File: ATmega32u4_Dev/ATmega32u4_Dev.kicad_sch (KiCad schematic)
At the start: 32 parts, among them J1 USB4105-GF-A, J2 ICSP HEader 2x3, J3 Conn_01x14_Pin, J4 Conn_01x14_Pin, SW1 1825910-6, U1 ATmega32U4-A, Y1 ABM8-16.000MHZ-10-1-U-T

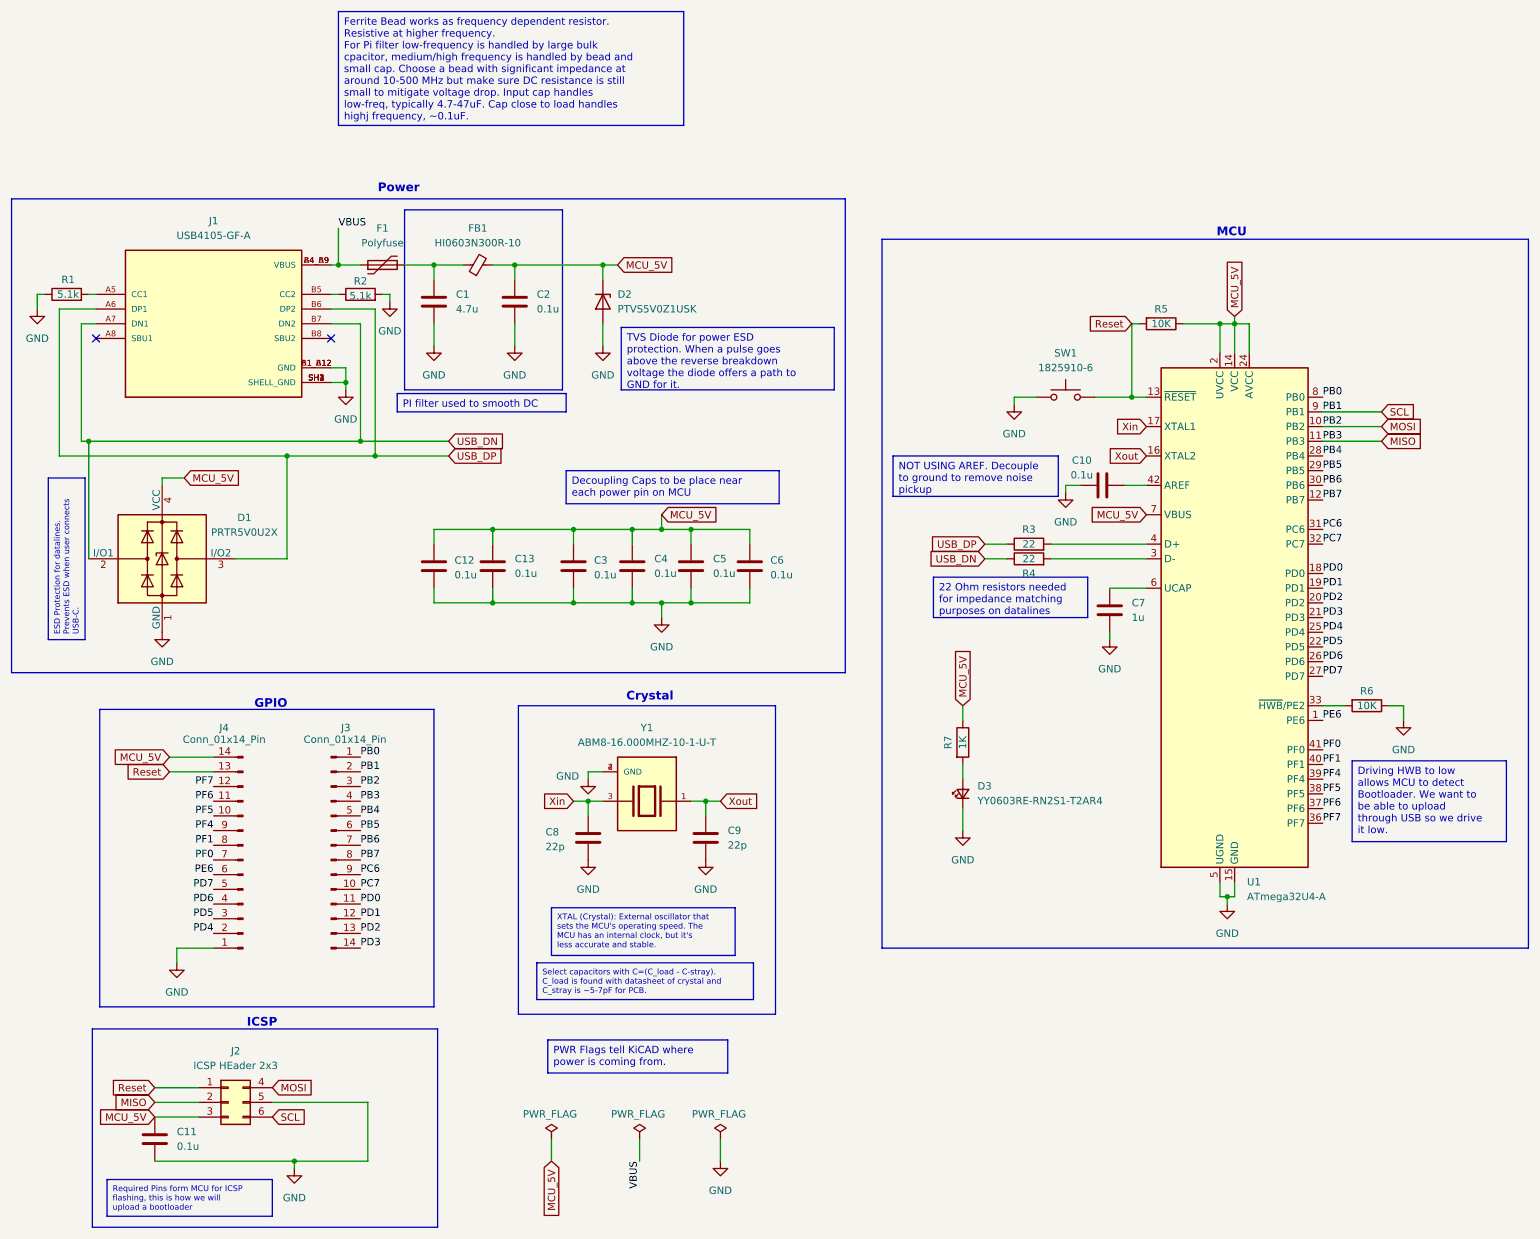
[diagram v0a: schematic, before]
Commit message: changed GPIO
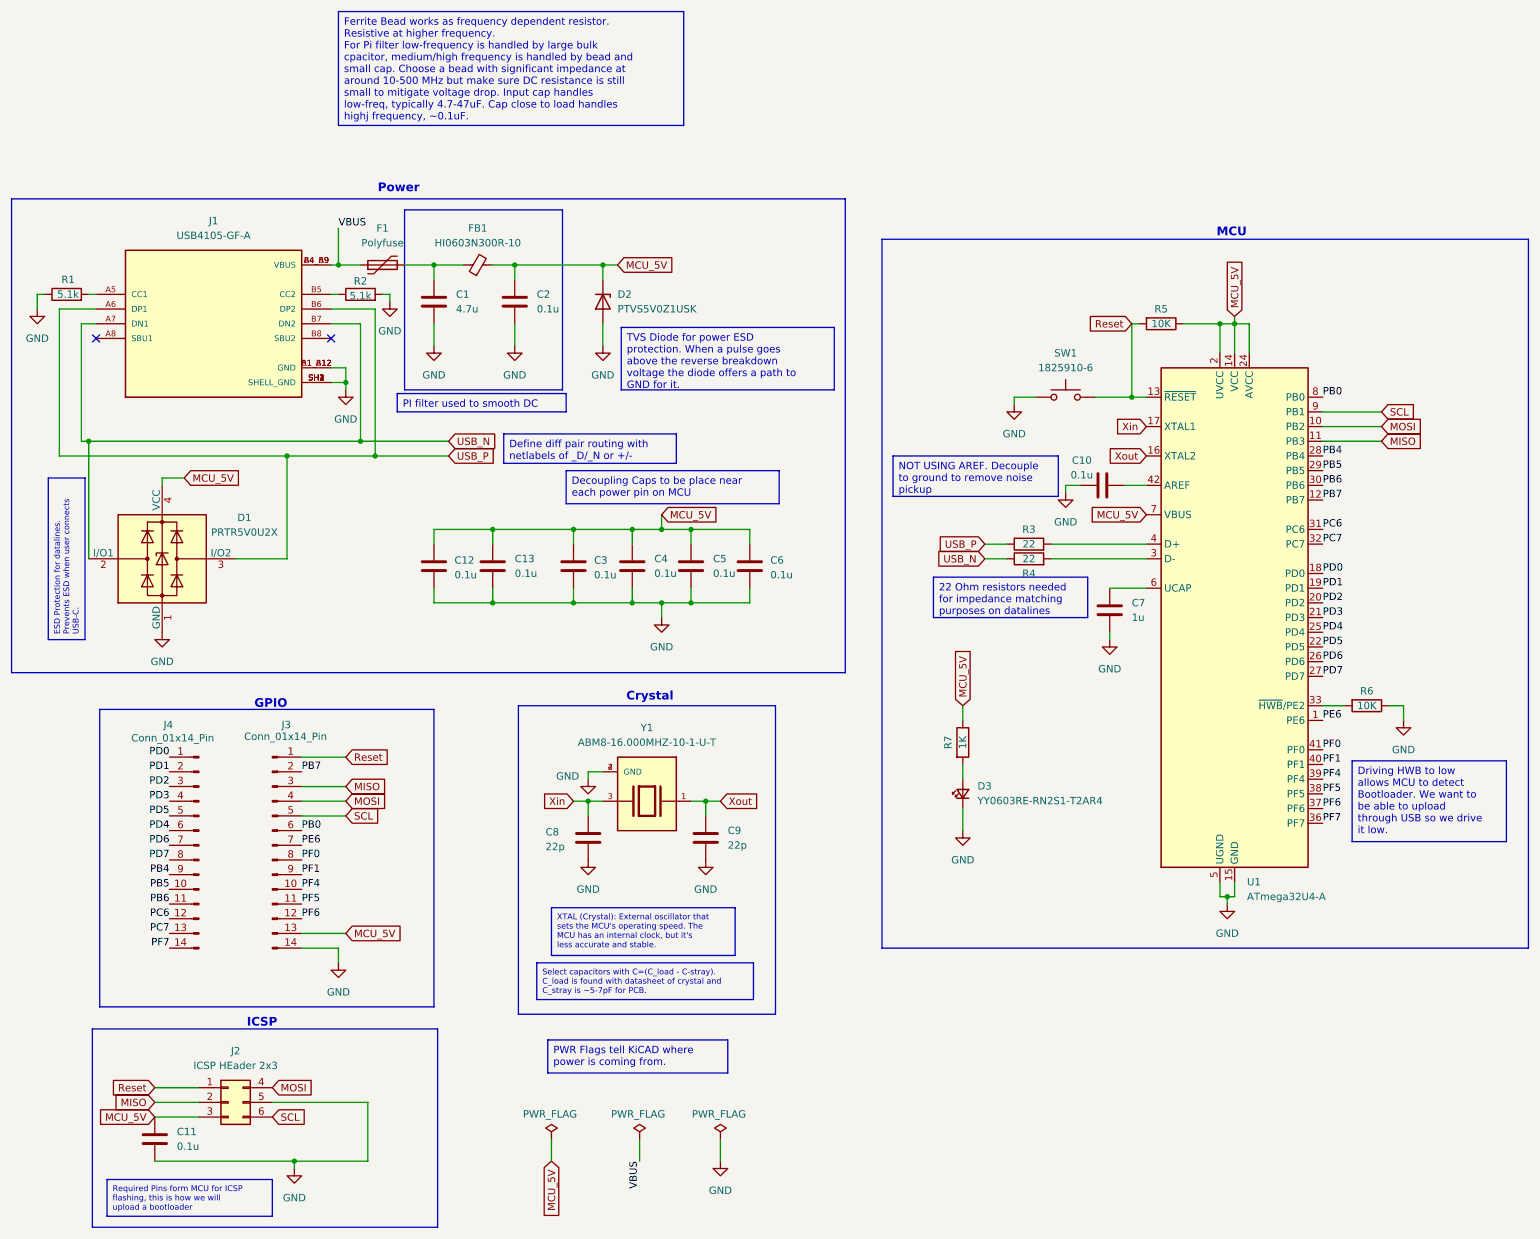
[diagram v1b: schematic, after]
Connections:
- net GND: now also J3.14 (Pin_14); no longer J4.1 (Pin_1)
- net MCU_5V: now also J3.13 (Pin_13); no longer J4.14 (Pin_14)
- net MISO: now also J3.3 (Pin_3); no longer J3.4 (Pin_4)
- net MOSI: now also J3.4 (Pin_4); no longer J3.3 (Pin_3)
- net PB0: now also J3.6 (Pin_6); no longer J3.1 (Pin_1)
- net PB4: now also J4.9 (Pin_9); no longer J3.5 (Pin_5)
- net PB5: now also J4.10 (Pin_10); no longer J3.6 (Pin_6)
- net PB6: now also J4.11 (Pin_11); no longer J3.7 (Pin_7)
- net PB7: now also J3.2 (Pin_2); no longer J3.8 (Pin_8)
- net PC6: now also J4.12 (Pin_12); no longer J3.9 (Pin_9)
- net PC7: now also J4.13 (Pin_13); no longer J3.10 (Pin_10)
- net PD0: now also J4.1 (Pin_1); no longer J3.11 (Pin_11)
- net PD1: now also J4.2 (Pin_2); no longer J3.12 (Pin_12)
- net PD2: now also J4.3 (Pin_3); no longer J3.13 (Pin_13)
- net PD3: now also J4.4 (Pin_4); no longer J3.14 (Pin_14)
- net PD4: now also J4.6 (Pin_6); no longer J4.2 (Pin_2)
- net PD5: now also J4.5 (Pin_5); no longer J4.3 (Pin_3)
- net PD6: now also J4.7 (Pin_7); no longer J4.4 (Pin_4)
- net PD7: now also J4.8 (Pin_8); no longer J4.5 (Pin_5)
- net PE6: now also J3.7 (Pin_7); no longer J4.6 (Pin_6)
- net PF0: now also J3.8 (Pin_8); no longer J4.7 (Pin_7)
- net PF1: now also J3.9 (Pin_9); no longer J4.8 (Pin_8)
- net PF4: now also J3.10 (Pin_10); no longer J4.9 (Pin_9)
- net PF5: now also J3.11 (Pin_11); no longer J4.10 (Pin_10)
- net PF6: now also J3.12 (Pin_12); no longer J4.11 (Pin_11)
- net PF7: now also J4.14 (Pin_14); no longer J4.12 (Pin_12)
- net Reset: now also J3.1 (Pin_1); no longer J4.13 (Pin_13)
- net SCL: now also J3.5 (Pin_5); no longer J3.2 (Pin_2)
- net USB_DN renamed USB_N
- net USB_DP renamed USB_P
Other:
- moved on the sheet: J3, J4

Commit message: Adjusted Layout
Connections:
- net USB_N: now also D1.3 (I/O2); no longer D1.2 (I/O1)
- net USB_P: now also D1.2 (I/O1); no longer D1.3 (I/O2)
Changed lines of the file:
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@@
+	)
+	(junction
+		(at 30.48 63.5)
+		(diameter 0)
+		(color 0 0 0 0)
 	)
 	(junction
@@
 	)
 	(junction
+		(at 64.77 60.96)
+		(diameter 0)
+		(color 0 0 0 0)
+	)
+	(junction
 		(at 74.93 50.8)
 		(diameter 0)
@@
 	)
 	(junction
-		(at 64.77 63.5)
-		(diameter 0)
-		(color 0 0 0 0)
-	)
-	(junction
 		(at 226.06 40.64)
 		(diameter 0)
@@
 	(junction
 		(at 90.17 30.48)
-		(diameter 0)
-		(color 0 0 0 0)
-	)
-	(junction
-		(at 30.48 60.96)
 		(diameter 0)
 		(color 0 0 0 0)
@@
 	(wire
 		(pts
+			(xy 55.88 81.28) (xy 64.77 81.28)
+		)
+		(stroke
+			(width 0)
+			(type default)
+		)
+	)
+	(wire
+		(pts
 			(xy 124.46 76.2) (xy 129.54 76.2)
 		)
@@
 	(wire
 		(pts
+			(xy 64.77 60.96) (xy 77.47 60.96)
+		)
+		(stroke
+			(width 0)
+			(type default)
+		)
+	)
+	(wire
+		(pts
 			(xy 129.54 73.66) (xy 129.54 76.2)
 		)
@@
 	(wire
 		(pts
-			(xy 29.21 60.96) (xy 30.48 60.96)
+			(xy 29.21 60.96) (xy 64.77 60.96)
 		)
 		(stroke
@@
 	(wire
 		(pts
-			(xy 64.77 63.5) (xy 80.01 63.5)
+			(xy 30.48 63.5) (xy 80.01 63.5)
 		)
 		(stroke
@@
 	(wire
 		(pts
-			(xy 64.77 81.28) (xy 64.77 63.5)
-		)
-		(stroke
-			(width 0)
-			(type default)
-		)
-	)
-	(wire
-		(pts
 			(xy 30.48 35.56) (xy 31.75 35.56)
 		)
@@
 	(wire
 		(pts
-			(xy 55.88 81.28) (xy 64.77 81.28)
-		)
-		(stroke
-			(width 0)
-			(type default)
-		)
-	)
-	(wire
-		(pts
 			(xy 80.01 63.5) (xy 92.71 63.5)
 		)
@@
 	(wire
 		(pts
+			(xy 64.77 60.96) (xy 64.77 81.28)
+		)
+		(stroke
+			(width 0)
+			(type default)
+		)
+	)
+	(wire
+		(pts
 			(xy 116.84 123.19) (xy 119.38 123.19)
 		)
@@
 	(wire
 		(pts
-			(xy 30.48 60.96) (xy 30.48 81.28)
-		)
-		(stroke
-			(width 0)
-			(type default)
-		)
-	)
-	(wire
-		(pts
 			(xy 137.16 123.19) (xy 137.16 125.73)
 		)
@@
 	(wire
 		(pts
-			(xy 25.4 63.5) (xy 64.77 63.5)
+			(xy 25.4 63.5) (xy 30.48 63.5)
 		)
 		(stroke
@@
 	(wire
 		(pts
+			(xy 30.48 63.5) (xy 30.48 81.28)
+		)
+		(stroke
+			(width 0)
+			(type default)
+		)
+	)
+	(wire
+		(pts
 			(xy 104.14 30.48) (xy 119.38 30.48)
 		)
@@
 		)
 		(stroke
-			(width 0)
-			(type default)
-		)
-	)
-	(wire
-		(pts
-			(xy 30.48 60.96) (xy 77.47 60.96)
-		)
-		(stroke

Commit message: V1
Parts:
- removed C2: 0.1u, Capacitor_SMD:C_0402_1005Metric, symbol Device:C
- removed D1: PRTR5V0U2X, Package_TO_SOT_SMD:SOT-143, symbol Power_Protection:PRTR5V0U2X
- added U2: USBLC6-2SC6, Package_TO_SOT_SMD:SOT-23-6, symbol Power_Protection:USBLC6-2SC6
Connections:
- net GND: now also J2.3 (Pin_3), J4.1 (Pin_1), U2.2 (GND); no longer J2.5 (Pin_5), J3.14 (Pin_14)
- net MCU_5V: now also J2.1 (Pin_1), J4.2 (Pin_2), U2.5 (VBUS); no longer J2.3 (Pin_3), J3.13 (Pin_13)
- net MISO: now also J2.6 (Pin_6), J3.11 (Pin_11); no longer J2.2 (Pin_2), J3.3 (Pin_3)
- net MOSI: now also J3.12 (Pin_12); no longer J3.4 (Pin_4)
- net PB0: now also J3.14 (Pin_14); no longer J3.6 (Pin_6)
- net PB4: now also J4.3 (Pin_3); no longer J4.9 (Pin_9)
- net PB5: now also J4.4 (Pin_4); no longer J4.10 (Pin_10)
- net PB6: now also J4.5 (Pin_5); no longer J4.11 (Pin_11)
- net PB7: now also J3.10 (Pin_10); no longer J3.2 (Pin_2)
- net PC6: now also J4.6 (Pin_6); no longer J4.12 (Pin_12)
- net PC7: now also J4.7 (Pin_7); no longer J4.13 (Pin_13)
- net PD0: now also J3.8 (Pin_8); no longer J4.1 (Pin_1)
- net PD1: now also J3.7 (Pin_7); no longer J4.2 (Pin_2)
- net PD2: now also J3.6 (Pin_6); no longer J4.3 (Pin_3)
- net PD3: now also J3.5 (Pin_5); no longer J4.4 (Pin_4)
- net PD4: now also J3.3 (Pin_3); no longer J4.6 (Pin_6)
- net PD5: now also J3.4 (Pin_4); no longer J4.5 (Pin_5)
- net PD6: now also J3.2 (Pin_2); no longer J4.7 (Pin_7)
- net PD7: now also J3.1 (Pin_1); no longer J4.8 (Pin_8)
- net PE6: now also J4.14 (Pin_14); no longer J3.7 (Pin_7)
- net PF0: now also J4.13 (Pin_13); no longer J3.8 (Pin_8)
- net PF1: now also J4.12 (Pin_12); no longer J3.9 (Pin_9)
- net PF4: now also J4.11 (Pin_11); no longer J3.10 (Pin_10)
- net PF5: now also J4.10 (Pin_10); no longer J3.11 (Pin_11)
- net PF6: now also J4.9 (Pin_9); no longer J3.12 (Pin_12)
- net PF7: now also J4.8 (Pin_8); no longer J4.14 (Pin_14)
- net Reset: now also J2.5 (Pin_5), J3.9 (Pin_9); no longer J2.1 (Pin_1), J3.1 (Pin_1)
- net SCL: now also J2.2 (Pin_2), J3.13 (Pin_13); no longer J2.6 (Pin_6), J3.5 (Pin_5)
- net USB_N: now also U2.6 (I/O1); no longer J1.A7 (DN1), J1.B7 (DN2)
- net USB_P: now also U2.4 (I/O2); no longer J1.A6 (DP1), J1.B6 (DP2)
- net Xin: now also C9.1, Y1.1; no longer C8.1, Y1.3
- net Xout: now also C8.1, Y1.3; no longer C9.1, Y1.1
- new net: J1.A6 (DP1), J1.B6 (DP2), U2.3 (I/O2)
- new net: J1.A7 (DN1), J1.B7 (DN2), U2.1 (I/O1)
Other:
- moved on the sheet: C11, D2
